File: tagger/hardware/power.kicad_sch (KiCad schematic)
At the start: 34 parts, among them J6 CHARGER, P1 USB, U12 TPS62A02DRL, U6 MAX77757JEFG420+T

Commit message: chore(tagger): schematic reorganization
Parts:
- J6: value CHARGER -> TETHER_POWER
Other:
- moved on the sheet: J6
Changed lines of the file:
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@@
 	(rectangle
 		(start 17.78 20.32)
-		(end 54.61 40.64)
+		(end 57.15 40.64)
 		(stroke
 			(width 0)
@@
 	(wire
 		(pts
-			(xy 41.91 30.48) (xy 41.91 33.02)
+			(xy 44.45 30.48) (xy 44.45 33.02)
 		)
 		(stroke
@@
 	(wire
 		(pts
-			(xy 39.37 30.48) (xy 41.91 30.48)
+			(xy 41.91 30.48) (xy 44.45 30.48)
 		)
 		(stroke
@@
 	(wire
 		(pts
-			(xy 39.37 27.94) (xy 74.93 27.94)
+			(xy 41.91 27.94) (xy 74.93 27.94)
 		)
 		(stroke
@@
 	)
 	(label "CHARGER"
-		(at 41.91 27.94 0)
+		(at 44.45 27.94 0)
 		(effects
 			(font
@@
 	(symbol
 		(lib_id "Connector:Conn_01x02_Socket")
-		(at 34.29 27.94 0)
+		(at 36.83 27.94 0)
 		(mirror y)
 		(unit 1)
@@
 		(dnp no)
 		(property "Reference" "J6"
-			(at 33.02 27.9399 0)
+			(at 35.56 27.9399 0)
 			(effects
 				(font
@@
 			)
 		)
-		(property "Value" "CHARGER"
-			(at 33.02 30.4799 0)
+		(property "Value" "TETHER_POWER"
+			(at 35.56 30.4799 0)
 			(effects
 				(font
@@
 		)
 		(property "Footprint" ""
-			(at 34.29 27.94 0)
+			(at 36.83 27.94 0)
 			(effects
 				(font
@@
 		)
 		(property "Datasheet" "~"
-			(at 34.29 27.94 0)
+			(at 36.83 27.94 0)
 			(effects
 				(font
@@
 		)
 		(property "Description" "Generic connector, single row, 01x02, script generated"
-			(at 34.29 27.94 0)
+			(at 36.83 27.94 0)
 			(effects
 				(font
@@
 		)
 		(property "Conn" "JST S02B-PASK-2"
-			(at 29.972 33.782 0)
+			(at 32.512 33.782 0)
 			(effects
 				(font
@@
 	(symbol
 		(lib_id "power:GND")
-		(at 41.91 33.02 0)
+		(at 44.45 33.02 0)
 		(unit 1)
 		(exclude_from_sim no)
@@
 		(dnp no)
 		(property "Reference" "#PWR016"
-			(at 41.91 39.37 0)
+			(at 44.45 39.37 0)
 			(effects
 				(font
@@
 		)
 		(property "Value" "GND"
-			(at 41.91 37.084 0)
+			(at 44.45 37.084 0)
 			(effects
 				(font
@@
 		)
 		(property "Footprint" ""
-			(at 41.91 33.02 0)
+			(at 44.45 33.02 0)
 			(effects
 				(font
@@
 		)
 		(property "Datasheet" ""
-			(at 41.91 33.02 0)
+			(at 44.45 33.02 0)
 			(effects
 				(font
@@
 		)
 		(property "Description" "Power symbol creates a global label with name \"GND\" , ground"
-			(at 41.91 33.02 0)
+			(at 44.45 33.02 0)
 			(effects
 				(font

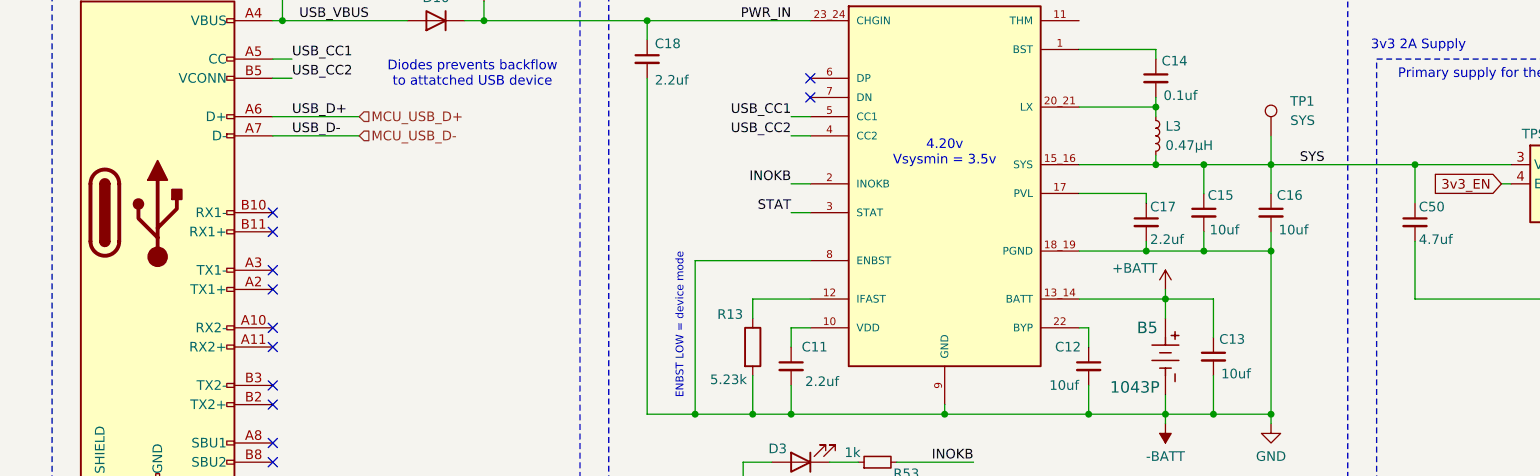
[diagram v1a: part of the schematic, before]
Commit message: feat(tagger): add notes to schematic
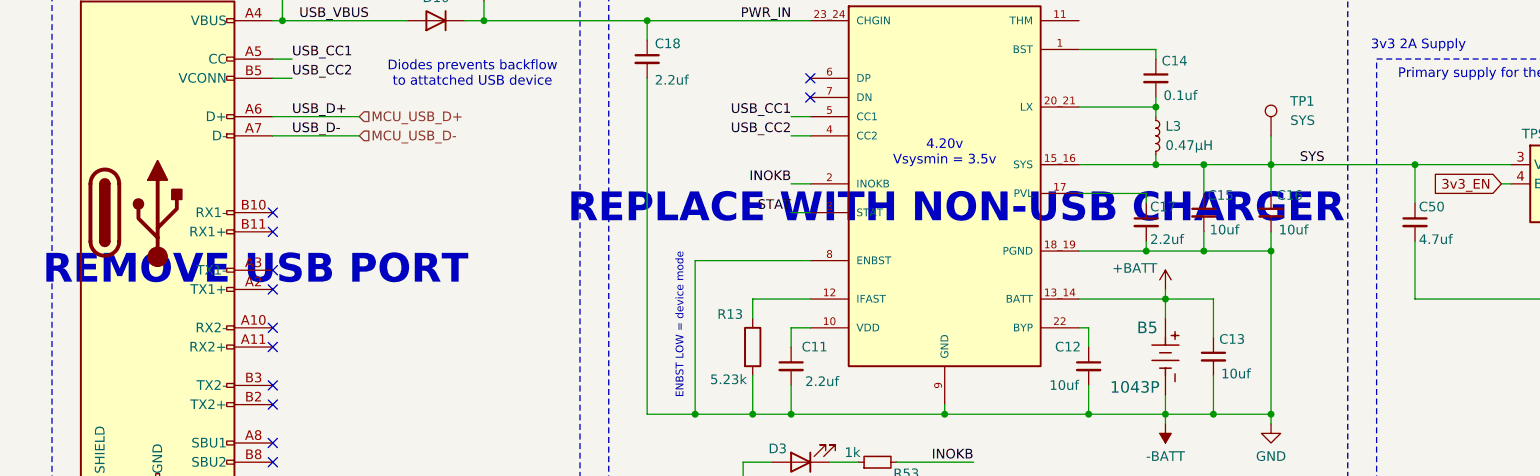
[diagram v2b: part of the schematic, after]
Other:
- note added: "REMOVE USB PORT"
- note added: "REPLACE WITH NON-USB CHARGER"
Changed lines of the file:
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@@
+		)
+	)
+	(text "REMOVE USB PORT"
+		(exclude_from_sim no)
+		(at 44.704 101.6 0)
+		(effects
+			(font
+				(size 3.81 3.81)
+				(thickness 0.762)
+				(bold yes)
+				(color 255 0 0 1)
+			)
 		)
 	)
@@
 			)
 		)
+	)
+	(text "REPLACE WITH NON-USB CHARGER"
+		(exclude_from_sim no)
+		(at 137.414 93.472 0)
+		(effects
+			(font
+				(size 3.81 3.81)
+				(thickness 0.762)
+				(bold yes)
+				(color 255 0 0 1)
+			)
+		)

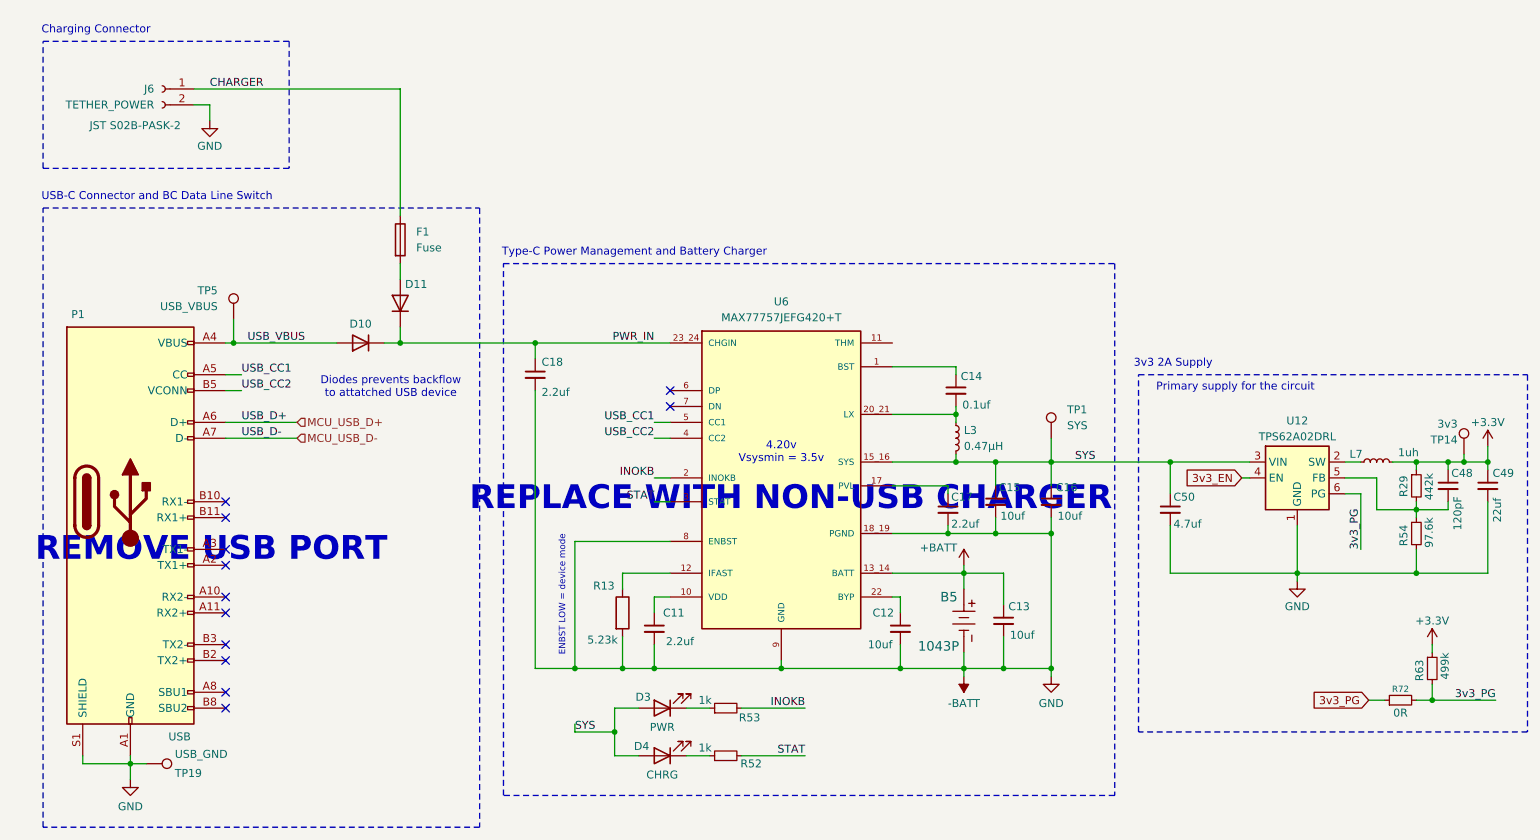
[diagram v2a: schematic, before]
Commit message: feat: schematic organization
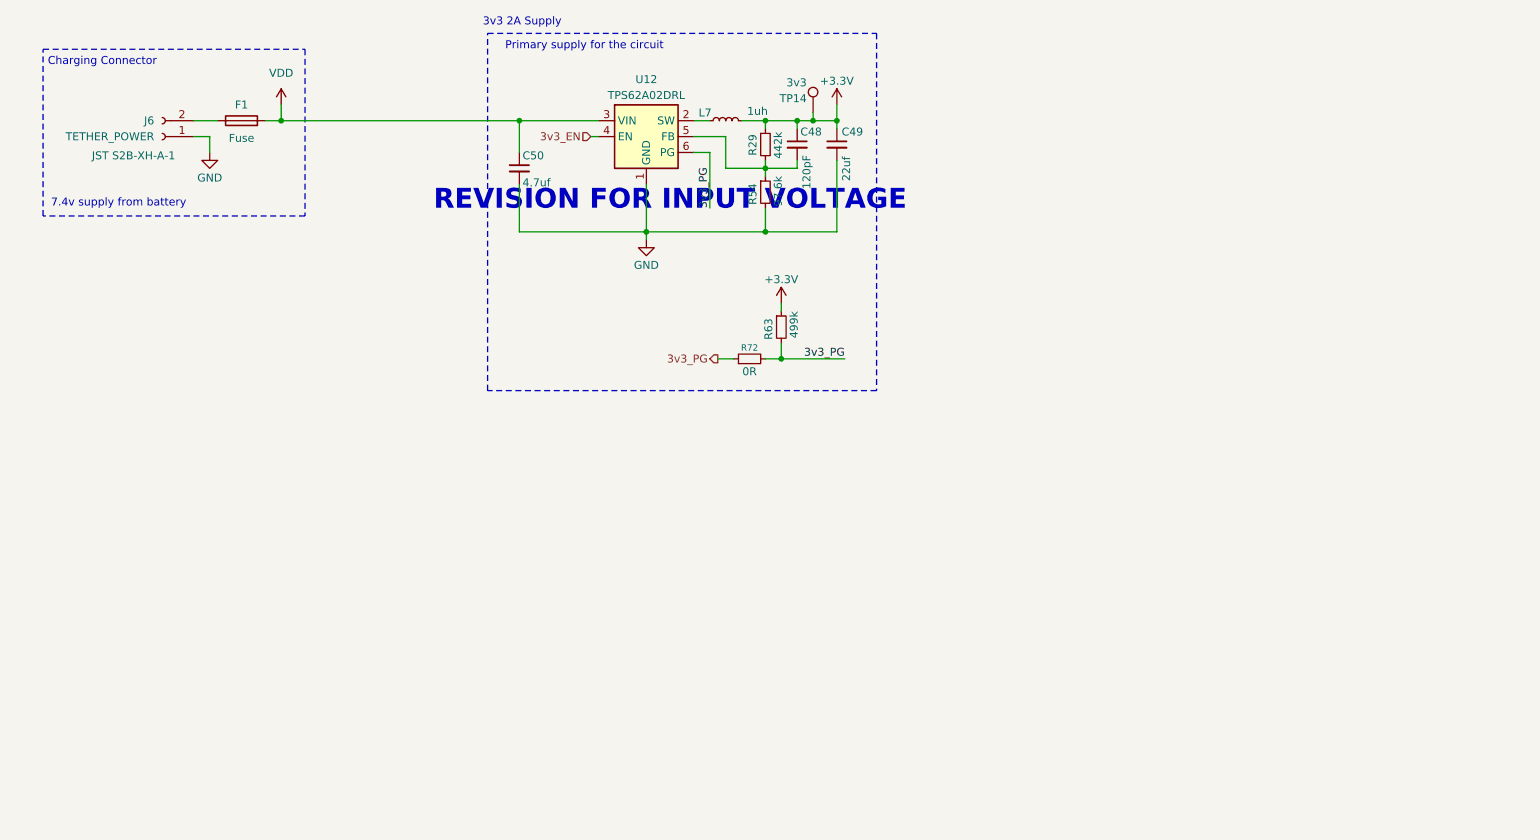
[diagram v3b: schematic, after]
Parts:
- removed B5: 1043P, BATT_1043P_KEY, symbol 2025-04-05_21-45-08:1043P
- removed C11, C17, C18: 2.2uf, symbol Device:C_Small
- removed C12, C13, C15, C16: 10uf, symbol Device:C_Small
- removed C14: 0.1uf, symbol Device:C_Small
- removed D10, D11: D, symbol Device:D
- removed D3: PWR, symbol Device:LED
- removed D4: CHRG, symbol Device:LED
- removed L3: 0.47µH, symbol Device:L_Small
- removed P1: USB, symbol Connector:USB_C_Plug
- removed R13: 5.23k, symbol Device:R
- removed R52, R53: 1k, symbol Device:R_Small
- removed TP1: SYS, symbol Connector:TestPoint
- removed TP19: USB_GND, TestPoint:TestPoint_Pad_D2.5mm, symbol Connector:TestPoint
- removed TP5: USB_VBUS, symbol Connector:TestPoint
- removed U6: MAX77757JEFG420+T, MAX77757JEFG420_T:IC_MAX77757JEFG420_T, symbol MAX77757JEFG420_T:MAX77757JEFG420_T
- C48, C49, C50: footprint Capacitor_SMD:C_0805_2012Metric_Pad1.18x1.45mm_HandSolder -> Capacitor_SMD:C_0201_0603Metric_Pad0.64x0.40mm_HandSolder
- F1: footprint (none) -> Fuse:Fuse_0805_2012Metric
- J6: footprint (none) -> Connector_JST:JST_XH_S2B-XH-A-1_1x02_P2.50mm_Horizontal; Conn JST S02B-PASK-2 -> JST S2B-XH-A-1
- R72: footprint (none) -> Resistor_SMD:R_0603_1608Metric_Pad0.98x0.95mm_HandSolder
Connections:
- net SYS is gone; now on net VDD: C50.1, U12.3 (VIN)
- net VDD: now reaches F1.2
- net -BATT renamed GND
- net GND: now also J6.1 (Pin_1); no longer J6.2 (Pin_2)
- net CHARGER: no longer names the net of F1.1
- net CHARGER: now also J6.2 (Pin_2); no longer J6.1 (Pin_1)
- no-connect marks 12 -> 0
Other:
- note added: "7.4v supply from battery"
- note added: "REVISION FOR INPUT VOLTAGE"
- note removed: "4.20v Vsysmin = 3.5v"
- note removed: "Diodes prevents backflow to attatched USB device"
- note removed: "ENBST LOW = device mode"
- note removed: "REMOVE USB PORT"
- note removed: "REPLACE WITH NON-USB CHARGER"
- note removed: "Type-C Power Management and Battery Charger"
- note removed: "USB-C Connector and BC Data Line Switch"
- moved on the sheet: C48, C49, C50, F1, J6, L7, R29, R54, R63, R72, TP14, U12

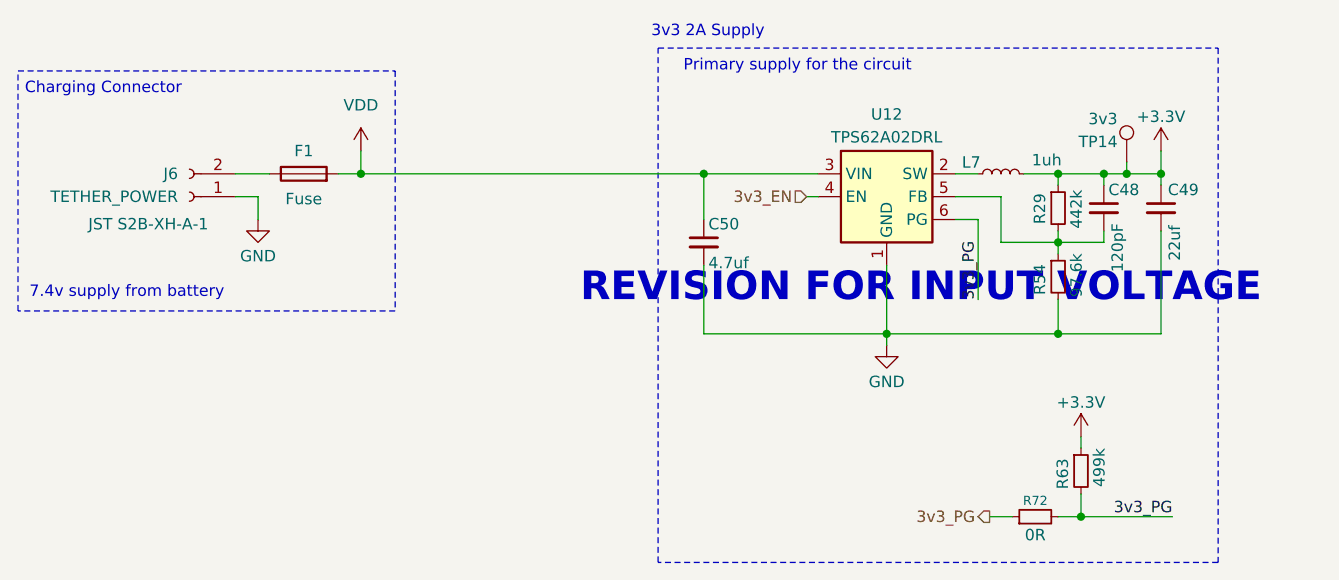
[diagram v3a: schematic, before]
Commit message: feat: board routing and RS485 implementation
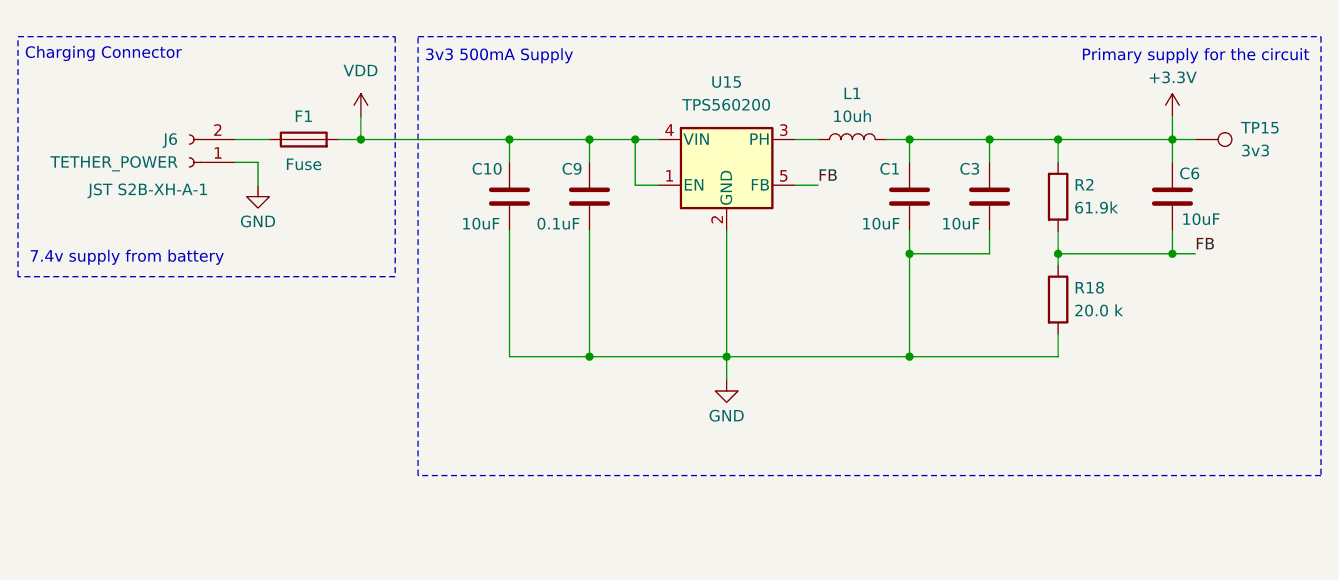
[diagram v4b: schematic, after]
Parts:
- removed C48: 120pF, Capacitor_SMD:C_0201_0603Metric_Pad0.64x0.40mm_HandSolder, symbol Device:C_Small
- removed C49: 22uf, Capacitor_SMD:C_0201_0603Metric_Pad0.64x0.40mm_HandSolder, symbol Device:C_Small
- removed C50: 4.7uf, Capacitor_SMD:C_0201_0603Metric_Pad0.64x0.40mm_HandSolder, symbol Device:C_Small
- removed L7: 1uh, symbol Device:L_Small
- removed R29: 442k, Resistor_SMD:R_0603_1608Metric_Pad0.98x0.95mm_HandSolder, symbol Device:R_Small
- removed R54: 97.6k, Resistor_SMD:R_0603_1608Metric_Pad0.98x0.95mm_HandSolder, symbol Device:R_Small
- removed R63: 499k, Resistor_SMD:R_0603_1608Metric_Pad0.98x0.95mm_HandSolder, symbol Device:R_Small
- removed R72: 0R, Resistor_SMD:R_0603_1608Metric_Pad0.98x0.95mm_HandSolder, symbol Device:R_Small
- removed TP14: 3v3, TestPoint:TestPoint_Pad_D2.5mm, symbol Connector:TestPoint
- removed U12: TPS62A02DRL, Package_TO_SOT_SMD:SOT-563, symbol Regulator_Switching:TPS62A02DRL
- added C1, C10, C3, C6: 10uF, Capacitor_SMD:C_0201_0603Metric_Pad0.64x0.40mm_HandSolder, symbol Device:C
- added C9: 0.1uF, Capacitor_SMD:C_0201_0603Metric_Pad0.64x0.40mm_HandSolder, symbol Device:C
- added L1: 10uh, Inductor_SMD:L_0603_1608Metric, symbol Device:L
- added R18: 20.0 k, Resistor_SMD:R_0201_0603Metric_Pad0.64x0.40mm_HandSolder, symbol Device:R
- added R2: 61.9k, Resistor_SMD:R_0201_0603Metric_Pad0.64x0.40mm_HandSolder, symbol Device:R
- added TP15: 3v3, TestPoint:TestPoint_Pad_D2.5mm, symbol Connector:TestPoint
- added U15: TPS560200, Package_TO_SOT_SMD:SOT-23-5, symbol Regulator_Switching:TPS560200
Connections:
- net +3.3V: now also C1.1, C3.1, C6.1, L1.2, R2.1, TP15.1
- net GND: now also C1.2, C10.2, C3.2, C9.2, R18.2, U15.2 (GND)
- net VDD: now also C10.1, C9.1, U15.1 (EN), U15.4 (VIN)
- new net: L1.1, U15.3 (PH)
- new net FB: C6.2, R18.1, R2.2, U15.5 (FB)
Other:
- note added: "3v3 500mA Supply"
- note removed: "3v3 2A Supply"
- note removed: "REVISION FOR INPUT VOLTAGE"
- moved on the sheet: F1, J6

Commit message: feat: more board layout
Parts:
- added TP16: VDD, TestPoint:TestPoint_Pad_D1.5mm, symbol Connector:TestPoint
- TP15: footprint TestPoint:TestPoint_Pad_D2.5mm -> TestPoint:TestPoint_Pad_D1.5mm
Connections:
- net VDD: now also TP16.1
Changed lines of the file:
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@@
+	(wire
+		(pts
+			(xy 55.88 29.21) (xy 55.88 31.75)
+		)
+		(stroke
+			(width 0)
+			(type default)
+		)
+	)
 	(wire
 		(pts
@@
 			)
 		)
-		(property "Footprint" "TestPoint:TestPoint_Pad_D2.5mm"
+		(property "Footprint" "TestPoint:TestPoint_Pad_D1.5mm"
 			(at 148.59 24.13 0)
 			(effects
@@
 					(unit 1)
 				)
+			)
+		)
+	)
+	(symbol
+		(lib_id "Connector:TestPoint")
+		(at 55.88 31.75 0)
+		(mirror x)
+		(unit 1)
+		(exclude_from_sim no)
+		(in_bom yes)
+		(on_board yes)
+		(dnp no)
+		(property "Reference" "TP16"
+			(at 49.53 35.306 0)
+			(effects
+				(font
+					(size 1.27 1.27)
+				)
+				(justify left)
+			)
+		)
+		(property "Value" "VDD"
+			(at 53.848 37.592 0)
+			(effects
+				(font
+					(size 1.27 1.27)
+				)
+				(justify left)
+			)
+		)
+		(property "Footprint" "TestPoint:TestPoint_Pad_D1.5mm"
+			(at 60.96 31.75 0)
+			(effects
+				(font
+					(size 1.27 1.27)
+				)
+				(hide yes)
+			)
+		)
+		(property "Datasheet" "~"
+			(at 60.96 31.75 0)
+			(effects
+				(font
+					(size 1.27 1.27)
+				)
+				(hide yes)
+			)
+		)
+		(property "Description" "test point"
+			(at 55.88 31.75 0)
+			(effects
+				(font
+					(size 1.27 1.27)
+				)
+				(hide yes)
+			)
+		)
+		(property "Height" ""
+			(at 55.88 31.75 0)
+			(effects
+				(font
+					(size 1.27 1.27)
+				)
+			)
+		)
+		(property "Manufacturer_Name" ""
+			(at 55.88 31.75 0)
+			(effects
+				(font
+					(size 1.27 1.27)
+				)
+			)
+		)
+		(property "Manufacturer_Part_Number" ""
+			(at 55.88 31.75 0)
+			(effects
+				(font
+					(size 1.27 1.27)
+				)
+			)
+		)
+		(property "Mouser Part Number" ""
+			(at 55.88 31.75 0)
+			(effects
+				(font
+					(size 1.27 1.27)
+				)
+			)
+		)
+		(property "Mouser Price/Stock" ""
+			(at 55.88 31.75 0)
+			(effects
+				(font
+					(size 1.27 1.27)
+				)
+			)
+		)
+		(property "JLC" ""
+			(at 55.88 31.75 0)
+			(effects
+				(font
+					(size 1.27 1.27)
+				)
+			)
+		)
+		(pin "1"
+		)
+		(instances
+			(project "tagger"
+				(path "/7f9981c1-8446-4881-979b-6d88a629918c/71e7c18f-1f33-427d-8bd6-9eec09af0cc4"
+					(reference "TP16")
+					(unit 1)
+				)

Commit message: feat: various board routing changes
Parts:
- added TP5: GND, TestPoint:TestPoint_Bridge_Pitch2.54mm_Drill1.0mm, symbol Connector:TestPoint
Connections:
- net GND: now also TP5.1
- net VDD: no longer U15.1 (EN)
- no-connect marks 0 -> 1
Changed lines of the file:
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@@
+	)
+	(junction
+		(at 72.39 53.34)
+		(diameter 0)
+		(color 0 0 0 0)
 	)
 	(junction
@@
 		(color 0 0 0 0)
 	)
-	(junction
-		(at 86.36 29.21)
-		(diameter 0)
-		(color 0 0 0 0)
+	(no_connect
+		(at 88.9 34.29)
 	)
 	(wire
@@
 	(wire
 		(pts
-			(xy 86.36 34.29) (xy 86.36 29.21)
-		)
-		(stroke
-			(width 0)
-			(type default)
-		)
-	)
-	(wire
-		(pts
 			(xy 133.35 41.91) (xy 133.35 43.18)
 		)
@@
 	(wire
 		(pts
-			(xy 88.9 34.29) (xy 86.36 34.29)
+			(xy 69.85 53.34) (xy 72.39 53.34)
 		)
 		(stroke
@@
 	(wire
 		(pts
-			(xy 86.36 29.21) (xy 81.28 29.21)
+			(xy 81.28 29.21) (xy 88.9 29.21)
 		)
 		(stroke
@@
 		(pts
 			(xy 116.84 41.91) (xy 116.84 53.34)
-		)
-		(stroke
-			(width 0)
-			(type default)
-		)
-	)
-	(wire
-		(pts
-			(xy 88.9 29.21) (xy 86.36 29.21)
 		)
 		(stroke
@@
 					(unit 1)
 				)
+			)
+		)
+	)
+	(symbol
+		(lib_id "Connector:TestPoint")
+		(at 69.85 53.34 90)
+		(unit 1)
+		(exclude_from_sim no)
+		(in_bom yes)
+		(on_board yes)
+		(dnp no)
+		(property "Reference" "TP5"
+			(at 68.326 51.308 90)
+			(effects
+				(font
+					(size 1.27 1.27)
+				)
+				(justify left)
+			)
+		)
+		(property "Value" "GND"
+			(at 68.58 55.626 90)
+			(effects
+				(font
+					(size 1.27 1.27)
+				)
+				(justify left)
+			)
+		)
+		(property "Footprint" "TestPoint:TestPoint_Bridge_Pitch2.54mm_Drill1.0mm"
+			(at 69.85 48.26 0)
+			(effects
+				(font
+					(size 1.27 1.27)
+				)
+				(hide yes)
+			)
+		)
+		(property "Datasheet" "~"
+			(at 69.85 48.26 0)
+			(effects
+				(font
+					(size 1.27 1.27)
+				)
+				(hide yes)
+			)
+		)
+		(property "Description" "test point"
+			(at 69.85 53.34 0)
+			(effects
+				(font
+					(size 1.27 1.27)
+				)
+				(hide yes)
+			)
+		)
+		(pin "1"
+		)
+		(instances
+			(project "tagger"
+				(path "/7f9981c1-8446-4881-979b-6d88a629918c/71e7c18f-1f33-427d-8bd6-9eec09af0cc4"
+					(reference "TP5")
+					(unit 1)
+				)
